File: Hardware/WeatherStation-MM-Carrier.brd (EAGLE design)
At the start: 58.4 x 54.6 mm, 148 parts, among them J11 microSD, J13 RJ11 - WIND, J2 JTAG, J3 QWIIC_RIGHT_ANGLE, J7 RJ11 - RAIN, J9 MICROMOD-2222-C, U1 BME280, U2 VEML6075, U3 AS3935, U5 AP7361C-33FGE

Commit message: Fix net names
Also renamed the sch/brd files to the right name
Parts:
- removed JP3: EN ADR PU, SparkFun-Jumpers:SMT-JUMPER_3_1-NC_TRACE_SILK
- removed R7: 4.7k, SparkFun-Resistors:0603
- added R21: 4.7k, SparkFun-Resistors:0603
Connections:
- removed net CAMERA_D0: J9.40
- removed net CAMERA_D1: J9.42
- removed net CAMERA_D2: J9.44
- removed net CAMERA_D3: J9.46
- removed net CAMERA_D4: J9.48
- removed net CAMERA_D5: J9.73
- removed net CAMERA_D6: J9.71
- removed net CAMERA_D7: J9.69
- removed net CAMERA_HSYNC: J9.63
- removed net CAMERA_I2C_SCL: J9.53
- removed net CAMERA_I2C_SDA: J9.51
- removed net CAMERA_INT: J9.16
- removed net CAMERA_MCLK: J9.58
- removed net CAMERA_PCLK: J9.56
- removed net CAMERA_TRIG: J9.67
- removed net CAMERA_VSYNC: J9.65
- removed net I2S_SCK/PDM_CLK: J9.50
- removed net I2S_SD: J9.54
- removed net I2S_WS/PDM_DAT: J9.52
- removed net N$8: JP3.3, R7.1
- removed net USBHOST_D+: J9.35
- removed net USBHOST_D-: J9.37
- new net N$19: R21.1, U1.2
- net 3.3V: now also R21.2; no longer R7.2, U1.2
- net A0: no longer J9.34
- net A1: no longer J9.38
- net BME_ADR: no longer JP3.2
- net D0: no longer J9.10
- net D1: no longer J9.18
- net GND: now also U3.15, U3.16; no longer JP3.1
- net LIGHTNING_INT: now also J9.40
- net PWM0: no longer J9.32
- net PWM1: no longer J9.47
- net RAIN: now also J9.44
- net RX1: no longer J9.19
- net RX2: no longer J9.20
- net SOIL_MOIST_SIG: now also J9.34
- net TX1: no longer J9.17
- net TX2: no longer J9.22
- net WDIR: now also J9.38
- net WSPEED: now also J9.42
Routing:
- net CAMERA_D1: track 46.7 -> 0.00 mm, vias 4 -> 0
- net CAMERA_INT: track 44.1 -> 0.00 mm, vias 2 -> 0
- net CAMERA_D3: track 43.8 -> 0.00 mm, vias 4 -> 0
- net CAMERA_MCLK: track 39.5 -> 0.00 mm, vias 2 -> 0
- net CAMERA_D2: track 39.3 -> 0.00 mm, vias 2 -> 0
- net CAMERA_D0: track 38.7 -> 0.00 mm, vias 2 -> 0
- net CAMERA_I2C_SCL: track 38.0 -> 0.00 mm, vias 2 -> 0
- net CAMERA_D4: track 37.5 -> 0.00 mm, vias 2 -> 0
- net CAMERA_I2C_SDA: track 37.5 -> 0.00 mm, vias 2 -> 0
- net CAMERA_PCLK: track 36.8 -> 0.00 mm, vias 2 -> 0
- net CAMERA_HSYNC: track 32.8 -> 0.00 mm, vias 2 -> 0
- net CAMERA_D5: track 32.4 -> 0.00 mm, vias 2 -> 0
- net CAMERA_TRIG: track 30.8 -> 0.00 mm, vias 2 -> 0
- net CAMERA_VSYNC: track 30.6 -> 0.00 mm, vias 2 -> 0
- net CAMERA_D6: track 28.6 -> 0.00 mm, vias 2 -> 0
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
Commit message: Final schematic changes from review and Nate's notes
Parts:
- removed D10, D3, D4, D5, D8, D9: 250mA/100V, SparkFun-DiscreteSemi:SOD-323
- removed R15, R16, R17: 1k, SparkFun-Resistors:0603
- removed R18: 4.7k, SparkFun-Resistors:0603
- added C10: 1.0uF, SparkFun-Capacitors:0603
- added C11: 0.22uF, SparkFun-Capacitors:0603
- added C12, C14: 0.1uF, SparkFun-Capacitors:0603
- added C9: 10uF, SparkFun-Capacitors:0603
- added R7: 10k, SparkFun-Resistors:0603
- JP2: value VIN LED ENABLE -> VIN LED
- JP4: value 3V3 LED ENABLE -> 3V3 LED
- R12, R13, R14: value 1k -> 10k
- R21: value 4.7k -> 10k
- moved R13 114.9 mm to (-68.6, -143.5)
- moved R12 107.3 mm to (-68.6, -132.1)
- moved R14 107.3 mm to (-68.6, -147.3)
- moved R21 7.62 mm to (-69.8, -116.8)
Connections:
- removed net 5V: D10.C, D3.C, D9.C, R18.2
- removed net BME_ADR: U1.5
- removed net N$12: J13.5, R14.1
- removed net N$13: J13.4, R15.1
- removed net N$17: J13.3, R16.1
- removed net N$18: J13.2, R17.1
- removed net N$7: J7.4, R12.2
- removed net N$9: J7.3, R13.2
- removed net RAIN2: J7.2
- removed net RAIN5: J7.5
- new net N$8: R7.1, U1.5
- new net SOIL_MOIST_PWR: J4.1, J9.46
- net 3.3V: now also R12.2, R13.2, R14.2, R7.2; no longer J4.1
- net GND: now also C10.2, C11.2, C12.2, C14.2, C9.2; no longer D4.A, D5.A, D8.A, R12.1, R14.2, R15.2
- net N$1: now also C10.1, C11.1, C9.1
- net RAIN: now also C12.1, J7.3, R12.1; no longer D3.A, D4.C, R13.1
- net WDIR: now also J13.2, R14.1; no longer D5.C, D9.A, R17.2, R18.1
- net WSPEED: now also C14.1, J13.3, R13.1; no longer D10.A, D8.C, R16.2

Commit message: Preliminary board layout
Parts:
- removed C12, C14: 0.1uF, SparkFun-Capacitors:0603
- removed LOGO1, LOGO4: SFE_LOGO_NAME_FLAME.1_INCH, SparkFun-Aesthetics:SFE_LOGO_NAME_FLAME_.1
- removed U$1: (no value), buzzard_labels (11):ACCEL6
- removed U$20: (no value), buzzard_labels (10):USB_HOST0
- removed U$22, U$65: (no value), buzzard_labels (11):MACHINE2
- removed U$24, U$64: (no value), buzzard_labels (11):MICROMOD0
- removed U$26: (no value), buzzard_labels (12):MICS0
- removed U$3: (no value), buzzard_labels (11):CAMERA5
- removed U$34: (no value), buzzard_labels (7):EN13
- removed U$35: (no value), buzzard_labels (7):EN24
- removed U$4, U$66: (no value), buzzard_labels (11):LEARNING3
- added D10, D3, D4, D5, D8, D9: 250mA/100V, SparkFun-DiscreteSemi:SOD-323
- moved R14 225.0 mm to (47.0, 45.7), turned to 90 degrees
- moved R13 217.2 mm to (38.1, 45.7), turned to 90 degrees
- moved R12 201.1 mm to (25.4, 45.7), turned to 90 degrees
- moved R21 196.3 mm to (58.4, 31.8)
- moved R7 187.5 mm to (50.8, 30.5), turned to 180 degrees
- moved L1 185.9 mm to (71.1, 36.8), turned to 90 degrees
- moved R19 182.4 mm to (61.0, 41.9), turned to 90 degrees
- moved R6 181.5 mm to (68.6, 36.8), turned to 270 degrees
- moved JP2 179.0 mm to (6.35, 58.4), flipped to the bottom, turned to 180 degrees
- moved R20 178.6 mm to (6.35, 58.4), turned to 180 degrees
- moved C8 178.0 mm to (67.3, 36.8), turned to 90 degrees
- moved D11 176.7 mm to (10.2, 58.4)
- moved C6 173.6 mm to (64.8, 40.6)
- moved C7 172.1 mm to (66.0, 33.0), turned to 270 degrees
- moved U3 164.1 mm to (62.2, 36.8), turned to 180 degrees
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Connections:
- removed net A0: J8.1
- removed net A1: J8.2
- net 3.3V: now also D3.C, D5.C, D9.C
- net D0: now also J9.10
- net D1: now also J9.18
- net GND: now also D10.A, D4.A, D8.A, J13.4, J13.5, J7.4; no longer C12.2, C14.2
- net PWM0: now also J9.32
- net PWM1: now also J9.47
- net RAIN: now also D3.A, D4.C; no longer C12.1
- net RX1: now also J9.19
- net RX2: now also J9.20
- net SOIL_MOIST_SIG: now also J8.1
- net TX1: now also J9.17
- net TX2: now also J9.22
- net WDIR: now also D10.C, D9.A, J8.2
- net WSPEED: now also D5.A, D8.C; no longer C14.1
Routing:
- net SOIL_MOIST_SIG: track 0.00 -> 53.6 mm, vias 0 -> 2
- net WDIR: track 0.00 -> 52.6 mm, vias 0 -> 2
- net SD_DAT1: track 41.1 -> 84.2 mm
- net TX1: track 33.2 -> 0.00 mm, vias 1 -> 0
- net A0: track 31.0 -> 0.00 mm, vias 2 -> 0
- net RX1: track 30.9 -> 0.00 mm, vias 1 -> 0
- net A1: track 29.9 -> 0.00 mm, vias 2 -> 0
- net PWM0: track 36.5 -> 58.9 mm
- net D0: track 42.7 -> 63.6 mm
- net PWM1: track 41.9 -> 61.9 mm
- net SD_DAT3: track 32.8 -> 51.2 mm
- net SD_DAT2: track 32.8 -> 51.1 mm
- net SD_DAT0: track 40.7 -> 58.8 mm
- net SD_CLK: track 39.5 -> 57.5 mm
- net SD_CMD: track 36.3 -> 54.4 mm
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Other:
- board size 58.4 x 54.6 mm -> 73.7 x 64.8 mm

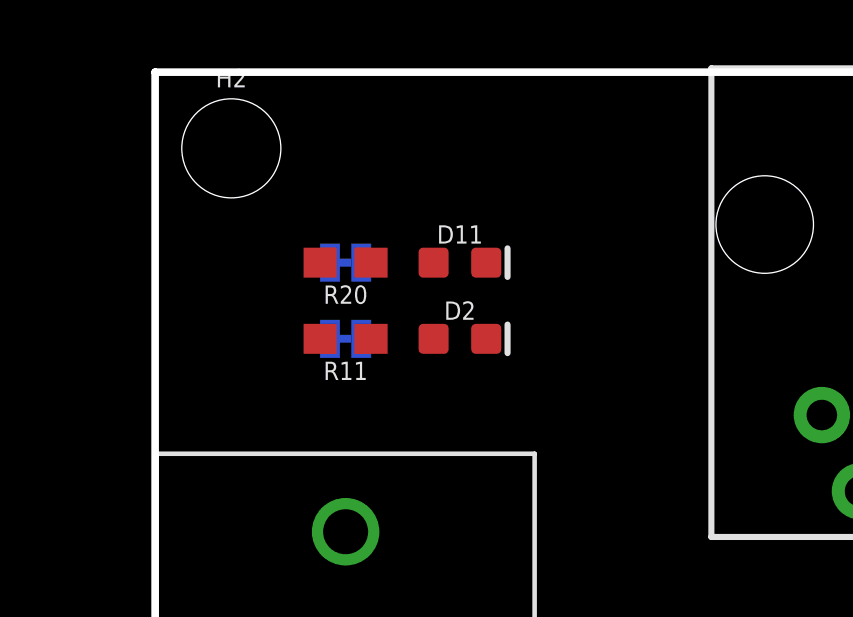
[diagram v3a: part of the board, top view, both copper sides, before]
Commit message: Moved power LEDs
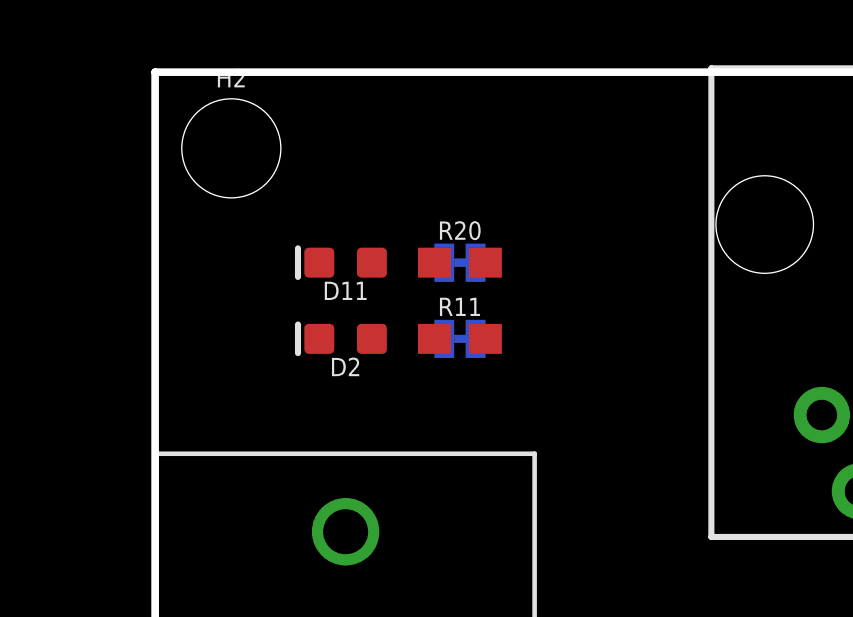
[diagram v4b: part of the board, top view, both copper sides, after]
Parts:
- moved D11 3.81 mm to (6.35, 58.4), turned to 180 degrees
- moved D2 3.81 mm to (6.35, 55.9), turned to 180 degrees
- moved JP2 3.81 mm to (10.2, 58.4), turned to 0 degrees
- moved JP4 3.81 mm to (10.2, 55.9), turned to 0 degrees
- moved R11 3.81 mm to (10.2, 55.9), turned to 0 degrees
- moved R20 3.81 mm to (10.2, 58.4), turned to 0 degrees

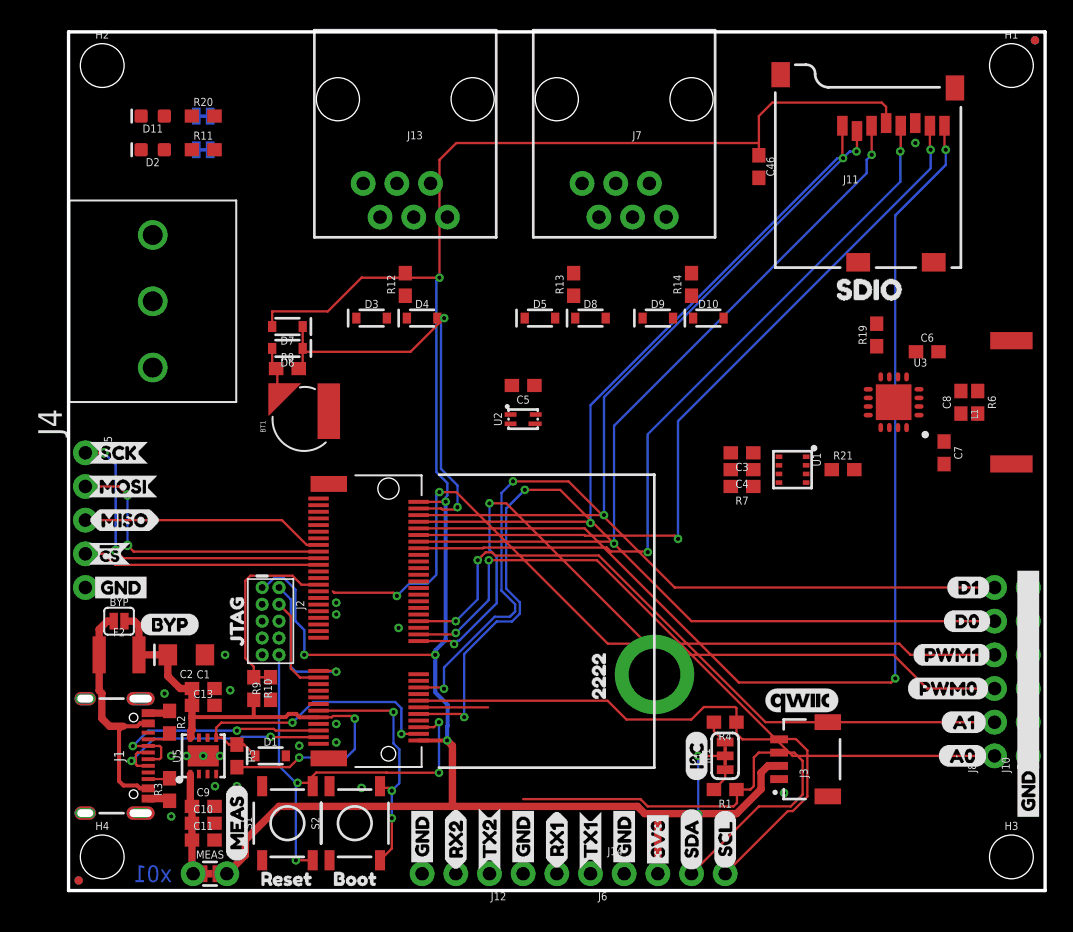
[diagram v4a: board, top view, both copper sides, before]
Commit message: Revised hardware layout
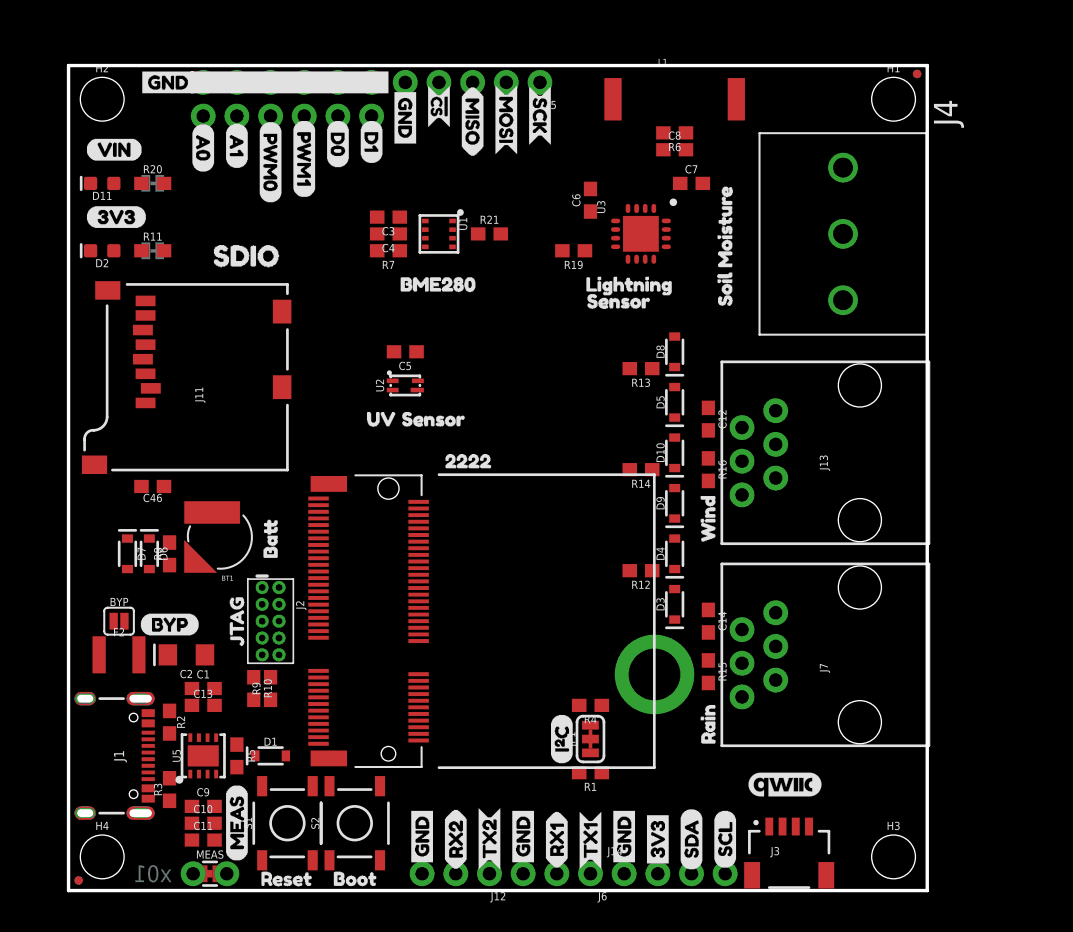
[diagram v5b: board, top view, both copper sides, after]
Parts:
- added C12, C14: 0.1uF, SparkFun-Capacitors:0603
- added R15, R16: 100k, SparkFun-Resistors:0603
- added U$1: (no value), buzzard_labels:VIN0
- added U$20: (no value), buzzard_labels:BME2805
- added U$22: (no value), buzzard_labels:LIGHTNING8
- added U$24: (no value), buzzard_labels:RAIN2
- added U$26, U$34: (no value), buzzard_labels:SENSOR7
- added U$35: (no value), buzzard_labels:SOIL_MOISTURE9
- added U$4: (no value), buzzard_labels:BATT4
- added U$62: (no value), buzzard_labels:UV6
- added U$63: (no value), buzzard_labels (1):3V30
- added U$64: (no value), buzzard_labels (1):WIND1
- moved U$11 87.5 mm to (5.08, 61.0), flipped to the bottom, turned to 180 degrees
- moved U$54 87.5 mm to (5.08, 61.0), flipped to the top, turned to 0 degrees
- moved J10 80.3 mm to (10.2, 61.0), flipped to the bottom, turned to 180 degrees
- moved J8 76.8 mm to (10.2, 58.4), flipped to the bottom, turned to 180 degrees
- moved U$44 76.0 mm to (10.2, 57.9), flipped to the top, turned to 270 degrees
- moved U$58 72.5 mm to (12.7, 57.9), flipped to the top, turned to 270 degrees
- moved U$43 70.7 mm to (10.2, 54.1), flipped to the bottom, turned to 90 degrees
- moved U$60 69.1 mm to (15.2, 58.0), flipped to the top, turned to 270 degrees
- moved U$57 67.5 mm to (12.7, 54.4), flipped to the bottom, turned to 90 degrees
- moved U$61 65.7 mm to (17.8, 58.2), flipped to the top, turned to 270 degrees
- moved U$16 62.1 mm to (20.3, 58.2), flipped to the top, turned to 270 degrees
- moved U$59 60.4 mm to (15.2, 51.8), flipped to the bottom, turned to 90 degrees
- moved U$13 58.6 mm to (22.9, 58.2), flipped to the top, turned to 270 degrees
- moved U$15 57.3 mm to (17.8, 52.2), flipped to the bottom, turned to 90 degrees
- moved U$14 57.0 mm to (20.3, 54.5), flipped to the bottom, turned to 90 degrees
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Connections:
- net 3.3V: now also R15.2, R16.2
- net GND: now also C12.1, C14.1
- net RAIN: now also C14.2, R15.1
- net WSPEED: now also C12.2, R16.1
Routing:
- net 3.3V: track 185.1 -> 0.00 mm, vias 7 -> 0
- net SD_DAT1: track 84.2 -> 0.00 mm, vias 2 -> 0
- net D0: track 63.6 -> 0.00 mm, vias 2 -> 0
- net PWM1: track 61.9 -> 0.00 mm, vias 2 -> 0
- net D1: track 60.9 -> 0.00 mm, vias 2 -> 0
- net PWM0: track 58.9 -> 0.00 mm, vias 2 -> 0
- net SD_DAT0: track 58.8 -> 0.00 mm, vias 2 -> 0
- net SD_CLK: track 57.5 -> 0.00 mm, vias 2 -> 0
- net SD_CMD: track 54.4 -> 0.00 mm, vias 2 -> 0
- net SOIL_MOIST_SIG: track 53.6 -> 0.00 mm, vias 2 -> 0
- net WDIR: track 52.6 -> 0.00 mm, vias 2 -> 0
- net SD_DAT3: track 51.2 -> 0.00 mm, vias 2 -> 0
- net SD_DAT2: track 51.1 -> 0.00 mm, vias 2 -> 0
- net I2C_SCL: track 44.9 -> 0.00 mm
- net I2C_SDA: track 43.8 -> 0.00 mm
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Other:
- board size 73.7 x 64.8 mm -> 64.8 x 62.2 mm

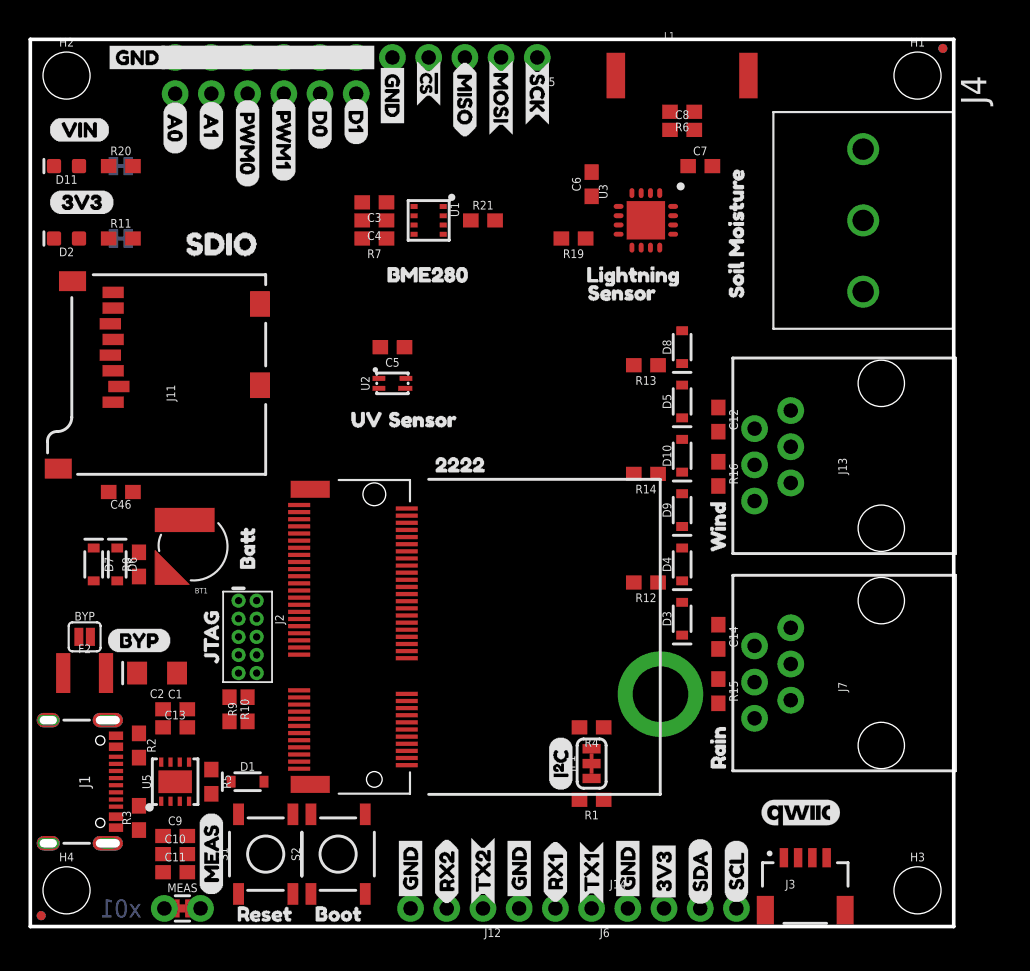
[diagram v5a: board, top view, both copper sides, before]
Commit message: Updated labels, condensed layout
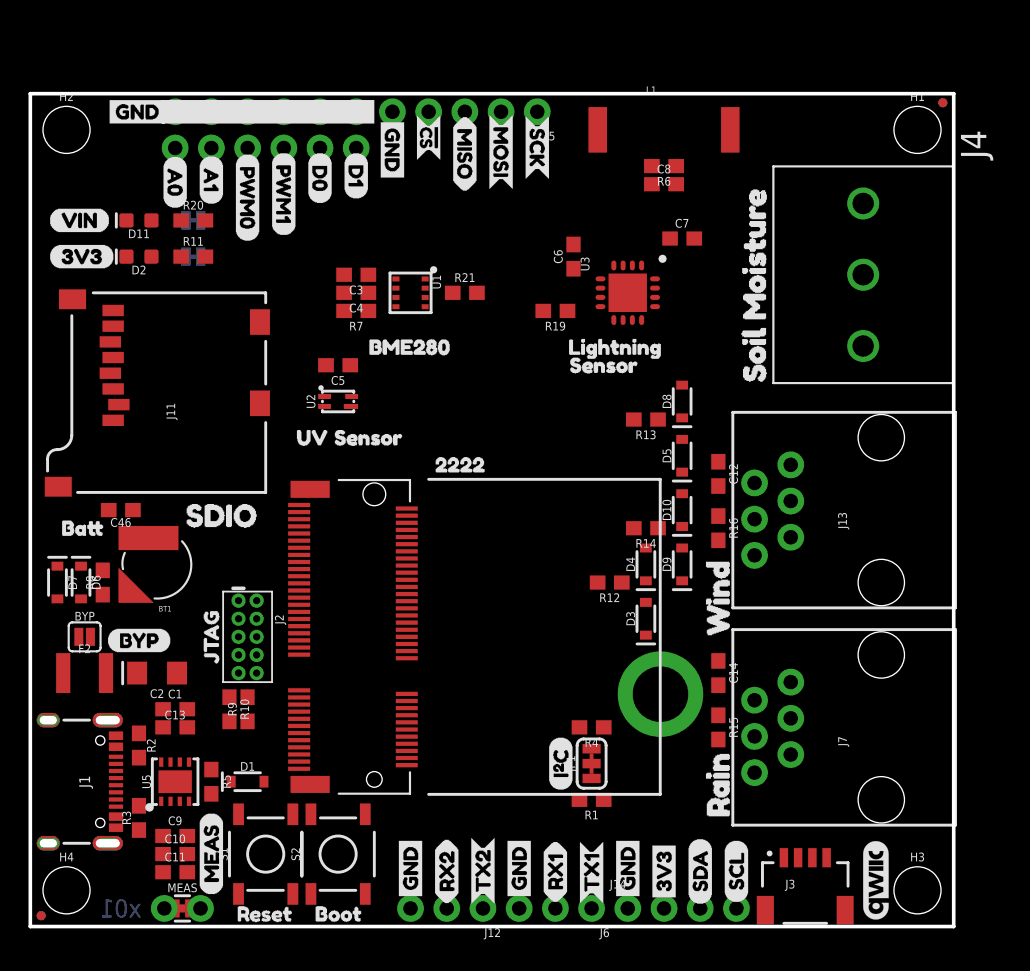
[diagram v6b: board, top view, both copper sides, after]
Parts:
- removed U$24: (no value), buzzard_labels:RAIN2
- removed U$35: (no value), buzzard_labels:SOIL_MOISTURE9
- removed U$64: (no value), buzzard_labels (1):WIND1
- added U$3: (no value), buzzard_labels (2):RAIN1
- added U$65: (no value), buzzard_labels (2):SOIL_MOISTURE2
- added U$66: (no value), buzzard_labels (2):WIND0
- moved U$21 19.0 mm to (9.53, 28.8)
- moved U$4 14.5 mm to (1.27, 27.9), turned to 0 degrees
- moved LOGO2 7.10 mm to (59.3, 3.24), turned to 90 degrees
- moved D11 6.35 mm to (7.62, 49.5)
- moved JP2 6.35 mm to (11.4, 49.5)
- moved R20 6.35 mm to (11.4, 49.5)
- moved U$1 6.35 mm to (1.27, 49.5)
- moved C7 5.24 mm to (45.7, 48.3)
- moved U$26 5.24 mm to (36.8, 39.4)
- moved R19 5.24 mm to (36.8, 43.2)
- moved U$22 5.24 mm to (36.8, 40.6)
- moved U3 5.24 mm to (41.9, 44.5)
- moved D2 5.24 mm to (7.62, 47.0)
- moved JP4 5.24 mm to (11.4, 47.0)
- moved R11 5.24 mm to (11.4, 47.0)
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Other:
- board size 64.8 x 62.2 mm -> 64.8 x 58.4 mm
